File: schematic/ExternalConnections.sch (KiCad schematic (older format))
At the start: 28 parts, among them J1 Radio_Jack, J2 User_Jack, J3 nanoESP32-S3-Left, J4 nanoESP32-S3-Right, Q1 MBT3904DW1T1, Q2 MBT3904DW1T1, Q3 MBT3904DW1T1, SW1 PTT_Button, SW2 Mode_Button, SW3 Vol_Up_Button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

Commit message: BOM for D2 has the wrong sized LED, updated to fix.
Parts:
- D2: LCSC C916073 -> C165982
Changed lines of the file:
@@
 F 1 "SYNC_LED" V 3438 3330 50  0000 L CNN
 F 2 "Diode_SMD:D_0603_1608Metric" H 3400 3250 50  0001 C CNN
-F 3 "https://datasheet.lcsc.com/lcsc/2011131906_TUOZHAN-TZ-P2-0602GTS1-1-1T_C916073.pdf" H 3400 3250 50  0001 C CNN
-F 4 "C916073" H 3400 3250 50  0001 C CNN "LCSC"
+F 3 "https://datasheet.lcsc.com/lcsc/1811131221_BrtLed-Bright-LED-Elec-BL-HGE36G-AV-TRB_C165982.pdf" H 3400 3250 50  0001 C CNN
+F 4 "C165982" H 3400 3250 50  0001 C CNN "LCSC"
 	1    3400 3250
 	0    1    1    0

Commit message: Move I2C SCL to GPIO 45 to resolve #9.
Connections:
- net GPIO45 renamed GPIO45_TLV320_SCL
- net GPIO48_TLV320_SCL: no longer names the net of J4.6 (Pin_6)
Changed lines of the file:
@@
 NoConn ~ 8850 1150
 Text GLabel 10250 2350 2    50   BiDi ~ 0
-GPIO45
-Text GLabel 10250 2450 2    50   BiDi ~ 0
-GPIO48_TLV320_SCL
+GPIO45_TLV320_SCL
 Text GLabel 10250 2550 2    50   BiDi ~ 0
 GPIO47_TLV320_SDA
@@
 	10150 2550 10250 2550
 Wire Wire Line
-	10250 2450 10150 2450
-Wire Wire Line
 	10150 2350 10250 2350
 Wire Wire Line
@@
 Text GLabel 7650 5100 0    50   BiDi ~ 0
 GPIO35
-Text GLabel 7650 5200 0    50   BiDi ~ 0
-GPIO45
 Text GLabel 7650 5300 0    50   BiDi ~ 0
-GPIO48_TLV320_SCL
+GPIO45_TLV320_SCL
 Text GLabel 7650 5400 0    50   BiDi ~ 0
 GPIO47_TLV320_SDA
@@
 NoConn ~ 7650 5000
 NoConn ~ 7650 5100
-NoConn ~ 7650 5200
 Text GLabel 6850 1200 0    50   BiDi ~ 0
 3.3V
@@
 Wire Wire Line
 	8400 5400 7650 5400
+NoConn ~ 10150 2450
 $EndSCHEMATC

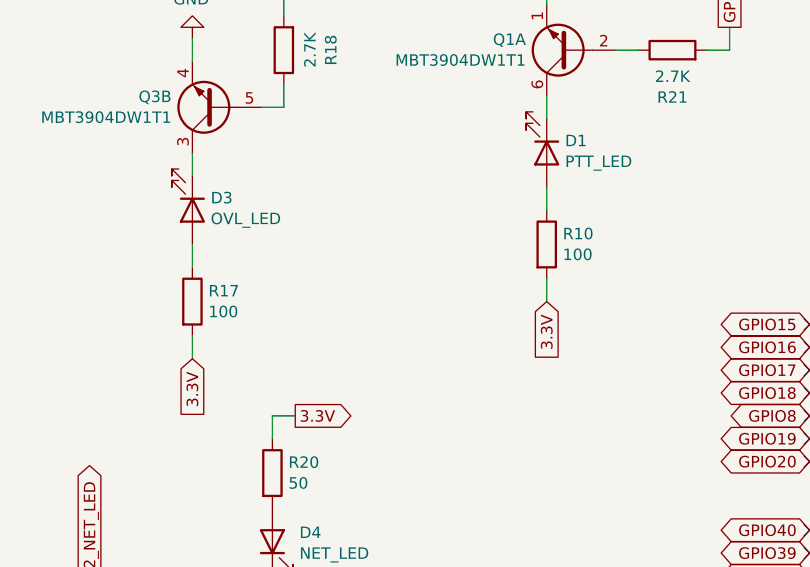
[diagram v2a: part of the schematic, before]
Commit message: Adjust R10 and R17 to match 20mA output current of other status LEDs. (#6)
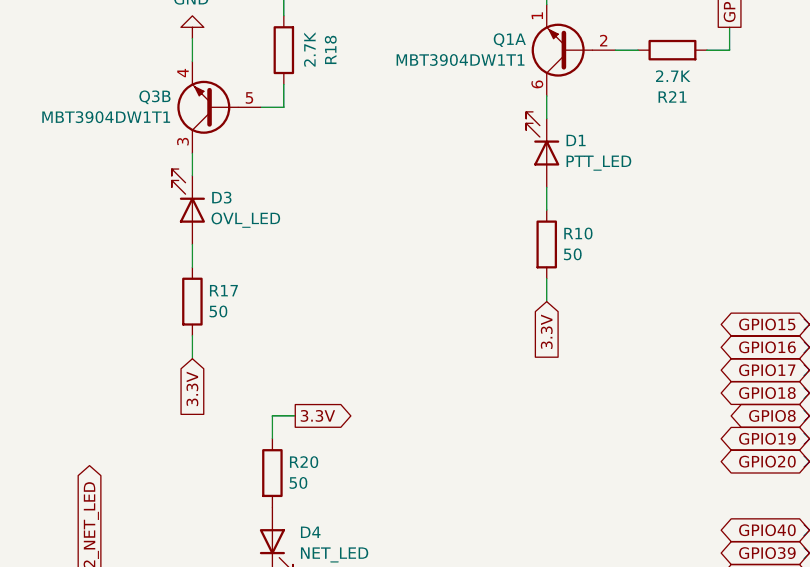
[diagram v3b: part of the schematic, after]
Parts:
- R10, R17: value 100 -> 50; LCSC C105588 -> C2759402
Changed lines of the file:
@@
 P 6500 3350
 F 0 "R10" H 6570 3396 50  0000 L CNN
-F 1 "100" H 6570 3305 50  0000 L CNN
+F 1 "50" H 6570 3305 50  0000 L CNN
 F 2 "Resistor_SMD:R_0603_1608Metric" V 6430 3350 50  0001 C CNN
-F 3 "https://datasheet.lcsc.com/lcsc/1810231425_YAGEO-RC0603FR-07100RL_C105588.pdf" H 6500 3350 50  0001 C CNN
-F 4 "C105588" H 6500 3350 50  0001 C CNN "LCSC"
+F 3 "https://datasheet.lcsc.com/lcsc/2103301905_UNI-ROYAL-Uniroyal-Elec-HP03W5F500JT5E_C2759402.pdf" H 6500 3350 50  0001 C CNN
+F 4 "C2759402" H 6500 3350 50  0001 C CNN "LCSC"
 	1    6500 3350
 	1    0    0    -1
@@
 P 4950 3600
 F 0 "R17" H 5020 3646 50  0000 L CNN
-F 1 "100" H 5020 3555 50  0000 L CNN
+F 1 "50" H 5020 3555 50  0000 L CNN
 F 2 "Resistor_SMD:R_0603_1608Metric" V 4880 3600 50  0001 C CNN
-F 3 "https://datasheet.lcsc.com/lcsc/1810231425_YAGEO-RC0603FR-07100RL_C105588.pdf" H 4950 3600 50  0001 C CNN
-F 4 "C105588" H 4950 3600 50  0001 C CNN "LCSC"
+F 3 "https://datasheet.lcsc.com/lcsc/2103301905_UNI-ROYAL-Uniroyal-Elec-HP03W5F500JT5E_C2759402.pdf" H 4950 3600 50  0001 C CNN
+F 4 "C2759402" H 4950 3600 50  0001 C CNN "LCSC"
 	1    4950 3600
 	1    0    0    -1

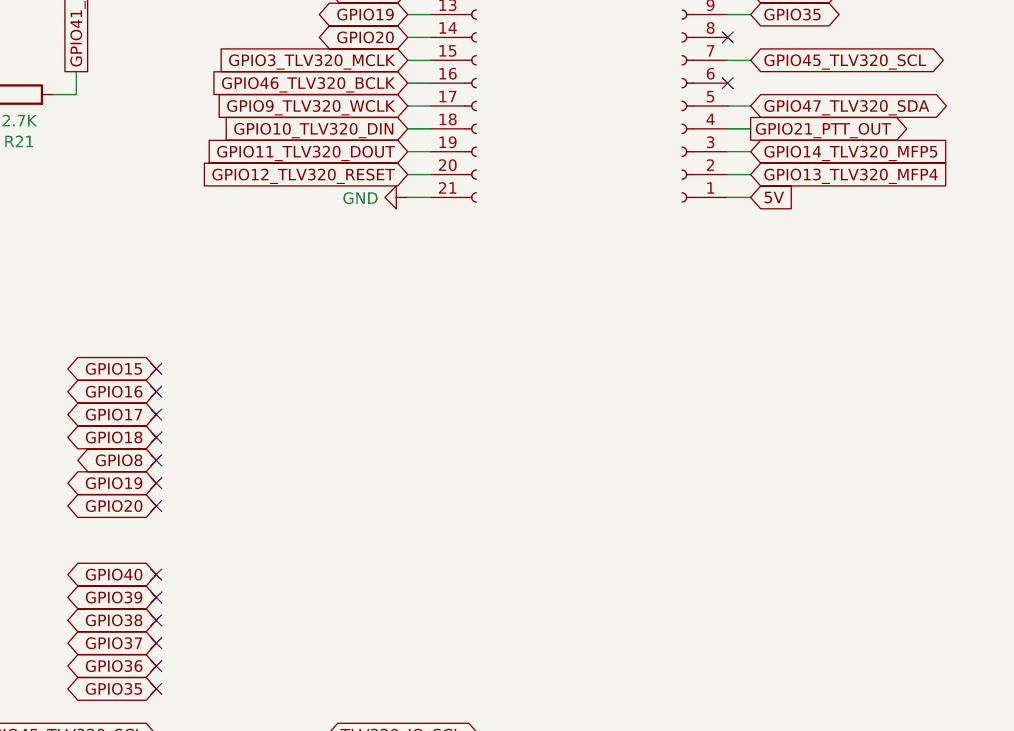
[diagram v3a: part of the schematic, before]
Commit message: Recreated dev platform PCB from scratch;
1. Swapped MFP4 and Reset for TLV320 for ease of routing. (#10)
2. Added vias around outside edge of board. (#1)
3. Added mounting holes for the dev board. (#5)
4. Moved silkscreen labels to improve readability. (#7)
5. Routed sensitive audio traces in inner layer and surrounded by ground vias/planes. (#10)
6. Set mic input capacitor values to same as used on TLV320 EVM to help with noise. (#10)
7. Replaced some parts with 0402 equivalents to help with positioning closer to TLV320. (#10)
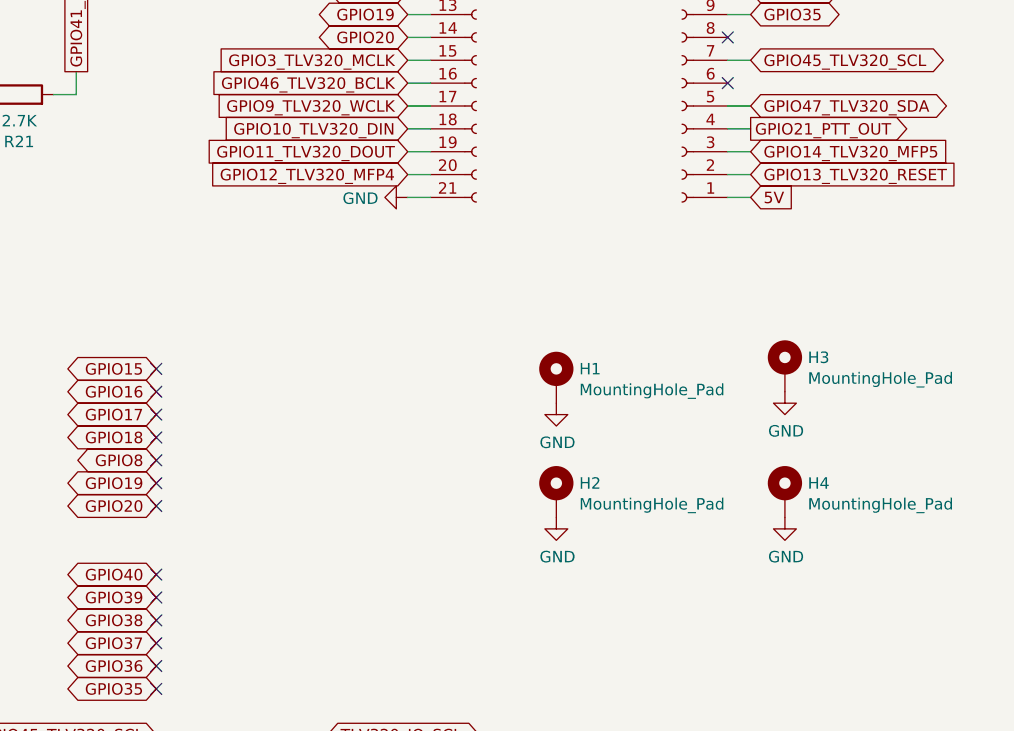
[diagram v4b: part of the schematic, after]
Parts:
- added H1, H2, H3, H4: MountingHole_Pad, MountingHole:MountingHole_3.2mm_M3_Pad, symbol Mechanical:MountingHole_Pad
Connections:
- net GND: now also H1.1, H2.1, H3.1, H4.1
- net GPIO12_TLV320_RESET renamed GPIO12_TLV320_MFP4
- net GPIO13_TLV320_MFP4 renamed GPIO13_TLV320_RESET
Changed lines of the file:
@@
 GPIO14_TLV320_MFP5
 Text GLabel 10250 2850 2    50   Input ~ 0
-GPIO13_TLV320_MFP4
+GPIO13_TLV320_RESET
 Text GLabel 10250 2950 2    50   Input ~ 0
 5V
@@
 GPIO11_TLV320_DOUT
 Text GLabel 8750 2850 0    50   Input ~ 0
-GPIO12_TLV320_RESET
+GPIO12_TLV320_MFP4
 Wire Wire Line
 	8850 950  8750 950
@@
 	8400 5400 7650 5400
 NoConn ~ 10150 2450
+$Comp
+L Mechanical:MountingHole_Pad H1
+U 1 1 629C4ADE
+P 9400 3750
+F 0 "H1" H 9500 3799 50  0000 L CNN
+F 1 "MountingHole_Pad" H 9500 3708 50  0000 L CNN
+F 2 "MountingHole:MountingHole_3.2mm_M3_Pad" H 9400 3750 50  0001 C CNN
+F 3 "~" H 9400 3750 50  0001 C CNN
+	1    9400 3750
+	1    0    0    -1
+$EndComp
+$Comp
+L Mechanical:MountingHole_Pad H3
+U 1 1 629C5347
+P 10400 3700
+F 0 "H3" H 10500 3749 50  0000 L CNN
+F 1 "MountingHole_Pad" H 10500 3658 50  0000 L CNN
+F 2 "MountingHole:MountingHole_3.2mm_M3_Pad" H 10400 3700 50  0001 C CNN
+F 3 "~" H 10400 3700 50  0001 C CNN
+	1    10400 3700
+	1    0    0    -1
+$EndComp
+$Comp
+L Mechanical:MountingHole_Pad H2
+U 1 1 629C5F2C
+P 9400 4250
+F 0 "H2" H 9500 4299 50  0000 L CNN
+F 1 "MountingHole_Pad" H 9500 4208 50  0000 L CNN
+F 2 "MountingHole:MountingHole_3.2mm_M3_Pad" H 9400 4250 50  0001 C CNN
+F 3 "~" H 9400 4250 50  0001 C CNN
+	1    9400 4250
+	1    0    0    -1
+$EndComp
+$Comp
+L Mechanical:MountingHole_Pad H4
+U 1 1 629C6C55
+P 10400 4250
+F 0 "H4" H 10500 4299 50  0000 L CNN
+F 1 "MountingHole_Pad" H 10500 4208 50  0000 L CNN
+F 2 "MountingHole:MountingHole_3.2mm_M3_Pad" H 10400 4250 50  0001 C CNN
+F 3 "~" H 10400 4250 50  0001 C CNN
+	1    10400 4250
+	1    0    0    -1
+$EndComp
+$Comp
+L power:GND #PWR06
+U 1 1 629C7681
+P 9400 3850
+F 0 "#PWR06" H 9400 3600 50  0001 C CNN
+F 1 "GND" H 9405 3677 50  0000 C CNN
+F 2 "" H 9400 3850 50  0001 C CNN
+F 3 "" H 9400 3850 50  0001 C CNN
+	1    9400 3850
+	1    0    0    -1
+$EndComp
+$Comp
+L power:GND #PWR08
+U 1 1 629C8134
+P 10400 3800
+F 0 "#PWR08" H 10400 3550 50  0001 C CNN
+F 1 "GND" H 10405 3627 50  0000 C CNN
+F 2 "" H 10400 3800 50  0001 C CNN
+F 3 "" H 10400 3800 50  0001 C CNN
+	1    10400 3800
+	1    0    0    -1
+$EndComp
+$Comp
+L power:GND #PWR07
+U 1 1 629C874D
+P 9400 4350
+F 0 "#PWR07" H 9400 4100 50  0001 C CNN
+F 1 "GND" H 9405 4177 50  0000 C CNN
+F 2 "" H 9400 4350 50  0001 C CNN
+F 3 "" H 9400 4350 50  0001 C CNN
+	1    9400 4350
+	1    0    0    -1
+$EndComp
+$Comp
+L power:GND #PWR09
+U 1 1 629C8D72
+P 10400 4350
+F 0 "#PWR09" H 10400 4100 50  0001 C CNN
+F 1 "GND" H 10405 4177 50  0000 C CNN
+F 2 "" H 10400 4350 50  0001 C CNN
+F 3 "" H 10400 4350 50  0001 C CNN
+	1    10400 4350
+	1    0    0    -1
+$EndComp
 $EndSCHEMATC
